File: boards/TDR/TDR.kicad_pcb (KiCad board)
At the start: 4 copper layers, 60 x 37 mm, 131 parts, among them J1 USB_C_Receptacle_USB2.0, J2 SMA, U1 LFE5UM5G-45-CABGA381, U10 W25Q128JVPIQ, U11 93LCxxBxxOT, U12 FT2232HL, U13 MIC5504-3.3YM5, U14 Resistive_Power_Divider, U15 MCP4822, U2 USBLC6-2SC6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

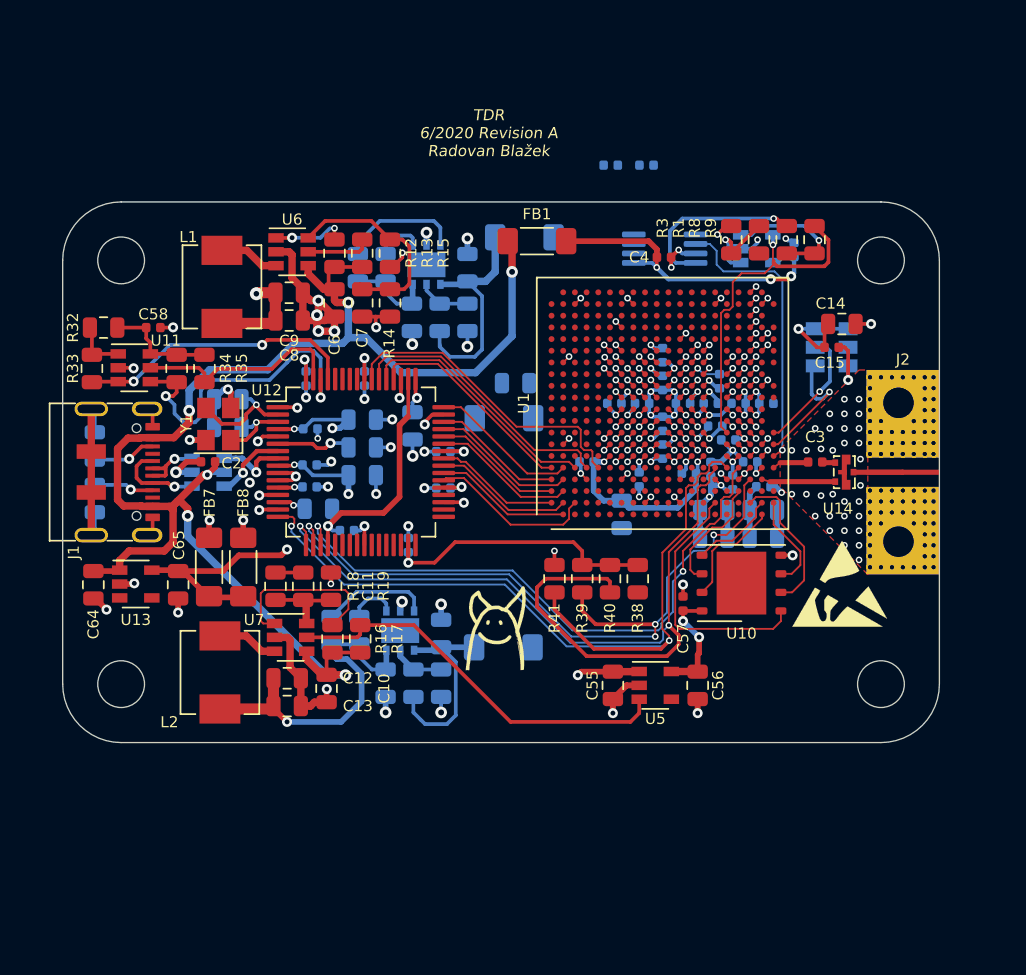
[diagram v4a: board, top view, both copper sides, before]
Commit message: solved DRC errors and routed few more nets
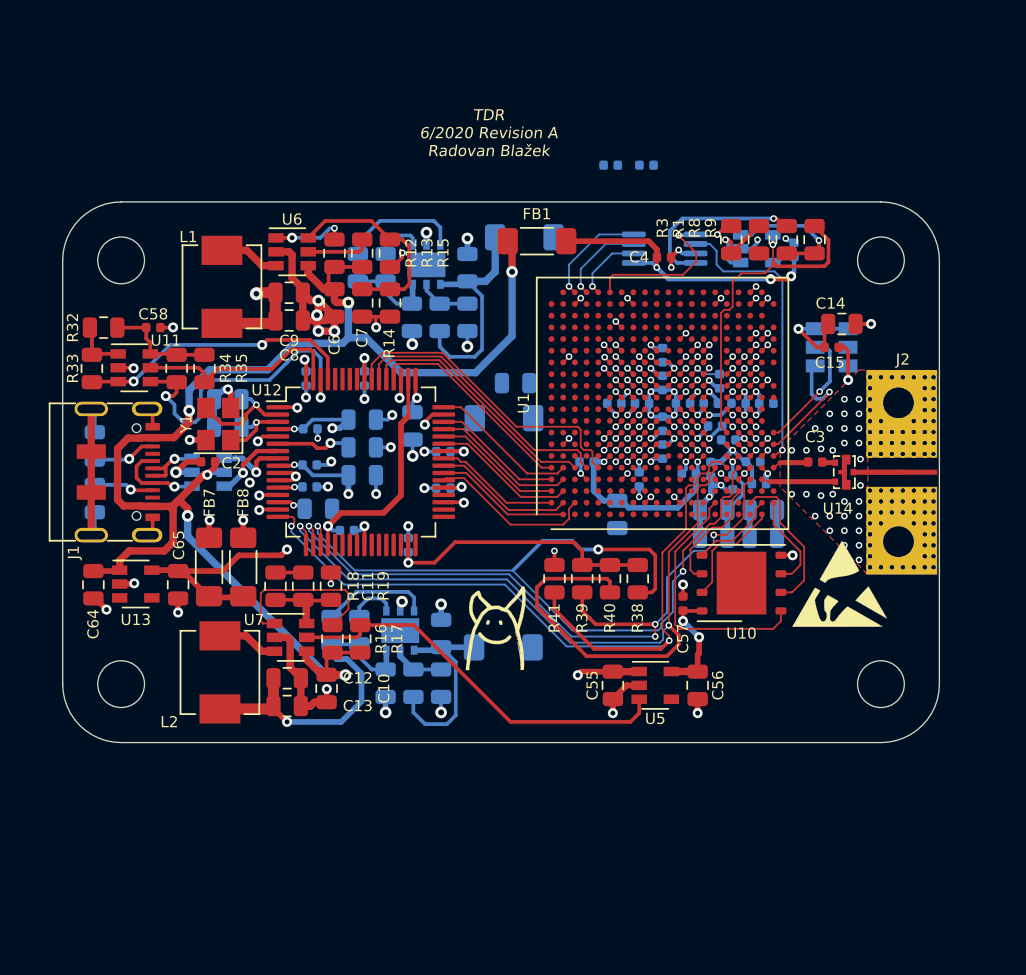
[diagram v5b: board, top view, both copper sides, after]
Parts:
- moved C34 1.84 mm to (154.3, 80.8)
- moved R2 1.62 mm to (154.7, 82.3)
- moved C45 0.30 mm to (145.0, 84.4)
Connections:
- U1 pad C20: Net-(U1-PadC20) -> /SCK
- U1 pad D20: Net-(U1-PadD20) -> /~LDAC
- U1 pad E20: Net-(U1-PadE20) -> /SDI
- U1 pad F10: /FPGA_IO/VCCIO0 -> Net-(U1-PadF10)
- U1 pad F11: /FPGA_IO/VCCIO1 -> Net-(U1-PadF11)
- U1 pad F12: /FPGA_IO/VCCIO1 -> Net-(U1-PadF12)
- U1 pad F20: Net-(U1-PadF20) -> /~CS
- U1 pad F9: /FPGA_IO/VCCIO0 -> Net-(U1-PadF9)
- U1 pad H14: /FPGA_IO/VCCIO2 -> +3V3
- U1 pad H15: /FPGA_IO/VCCIO2 -> +3V3
- U1 pad J15: /FPGA_IO/VCCIO2 -> +3V3
- U1 pad L14: /FPGA_IO/VCCIO3 -> Net-(U1-PadL14)
- U1 pad L15: /FPGA_IO/VCCIO3 -> Net-(U1-PadL15)
- U1 pad L6: /FPGA_IO/VCCIO6 -> Net-(U1-PadL6)
- U1 pad L7: /FPGA_IO/VCCIO6 -> Net-(U1-PadL7)
- U1 pad M15: /FPGA_IO/VCCIO3 -> Net-(U1-PadM15)
- U1 pad M6: /FPGA_IO/VCCIO6 -> Net-(U1-PadM6)
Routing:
- net /TMS: track 41.7 -> 56.3 mm, vias 2 -> 3
- net /~CS: track 0.00 -> 10.8 mm, vias 0 -> 1
- net /SCK: track 0.00 -> 7.35 mm, vias 0 -> 1
- net /~LDAC: track 0.00 -> 6.11 mm, vias 0 -> 1
- net /SDI: track 0.00 -> 4.86 mm, vias 0 -> 1
- net /VCCA: track 3.95 -> 7.12 mm
- net /FPGA_Power/VCCAUX: track 43.3 -> 41.4 mm, vias 8 -> 6
- net /FPGA_IO/VCCIO6: track 1.70 -> 0.00 mm, vias 2 -> 0
- net GND: track 184.6 -> 183.8 mm, vias 178 -> 177

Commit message: add LEDs, only 9 unconnected items remaining
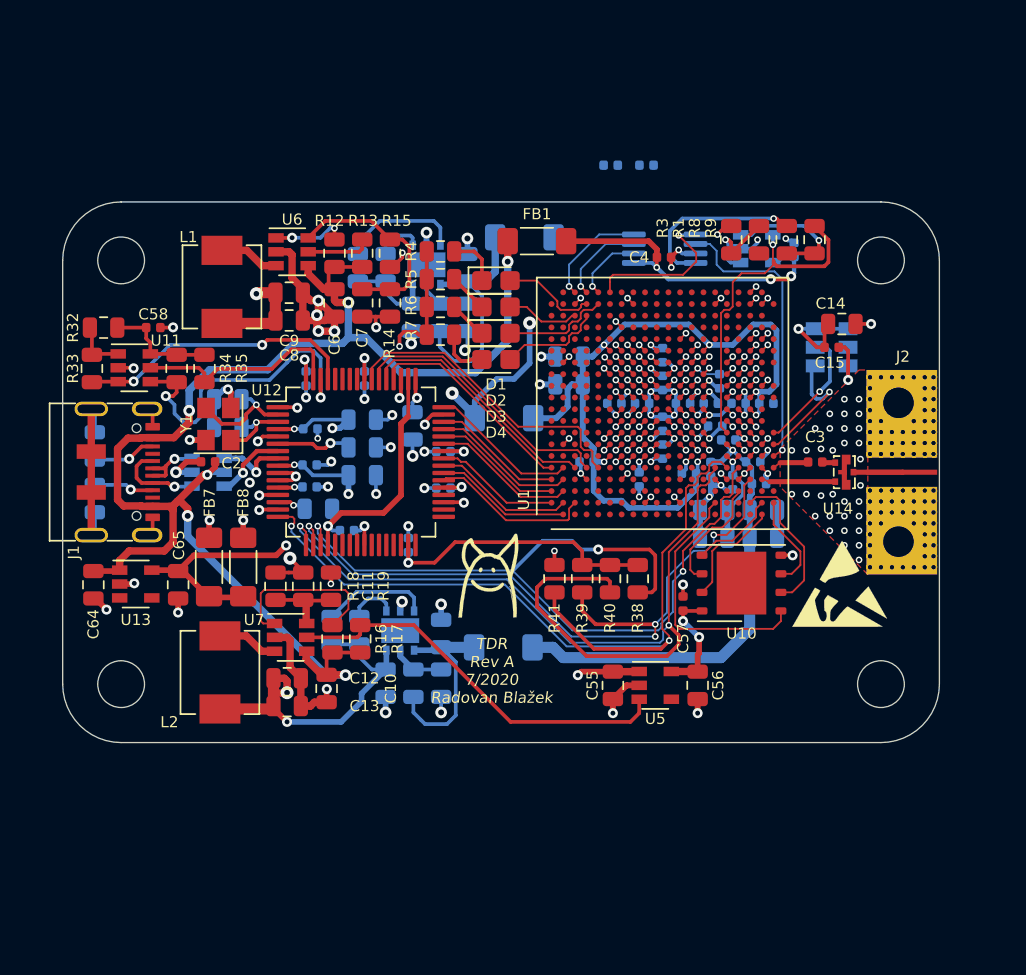
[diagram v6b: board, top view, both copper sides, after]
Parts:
- added D1: LED, LED_SMD:LED_0805_2012Metric_Castellated, F.Cu at (136.7, 68.4)
- added D2: LED, LED_SMD:LED_0805_2012Metric_Castellated, F.Cu at (136.7, 70.2)
- added D3: LED, LED_SMD:LED_0805_2012Metric_Castellated, F.Cu at (136.7, 72.0)
- added D4: LED, LED_SMD:LED_0805_2012Metric_Castellated, F.Cu at (136.7, 73.8)
- added R4: 1k, Resistor_SMD:R_0805_2012Metric, F.Cu at (132.9, 66.4)
- added R5: 1k, Resistor_SMD:R_0805_2012Metric, F.Cu at (132.9, 68.3)
- added R6: 1k, Resistor_SMD:R_0805_2012Metric, F.Cu at (132.9, 70.2)
- added R7: 1k, Resistor_SMD:R_0805_2012Metric, F.Cu at (132.9, 72.1)
- moved C45 9.49 mm to (141.7, 75.5), turned to 180 degrees
- moved C47 4.08 mm to (141.7, 73.6)
- moved G*** 3.63 mm to (136.2, 88.6)
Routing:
- net +2V5: track 39.7 -> 109.8 mm, vias 2 -> 6
- net VCCHTX: track 8.14 -> 32.1 mm
- net +3V3: track 37.3 -> 54.2 mm, vias 7 -> 10
- net GND: track 183.8 -> 195.3 mm, vias 177 -> 180
- net /FPGA_Power/VCCAUX: track 41.4 -> 52.7 mm
- net Net-(D3-Pad2): track 0.00 -> 7.32 mm
- net Net-(D4-Pad2): track 0.00 -> 7.07 mm
- net Net-(D1-Pad2): track 0.00 -> 6.54 mm
- net Net-(D2-Pad2): track 0.00 -> 5.02 mm
- net Net-(D1-Pad1): track 0.00 -> 3.59 mm
- net Net-(D4-Pad1): track 0.00 -> 3.47 mm
- net Net-(D2-Pad1): track 0.00 -> 2.69 mm
- net Net-(D3-Pad1): track 0.00 -> 2.65 mm
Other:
- board text added: "TDR Rev A 7/2020 Radovan Blažek"
- board text removed: "TDR 6/2020 Revision A Radovan Blažek"

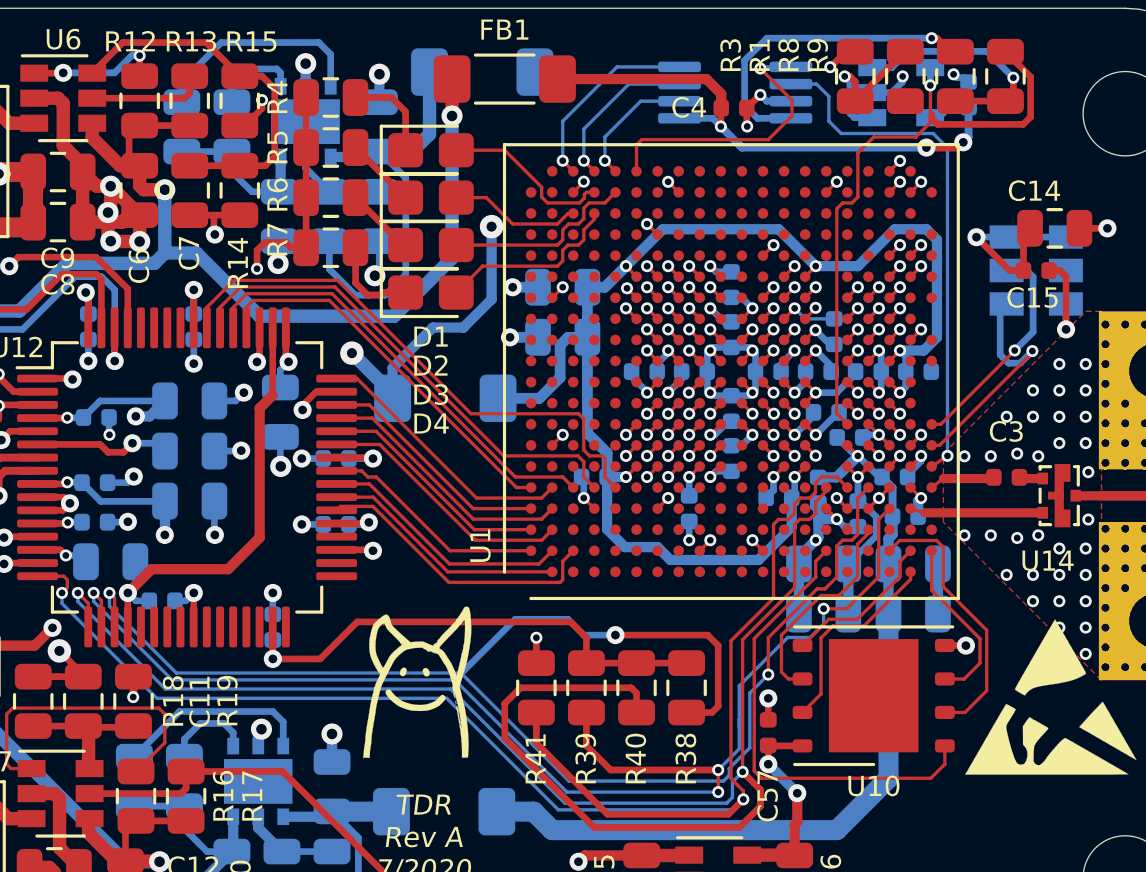
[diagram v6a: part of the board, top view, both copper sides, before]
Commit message: change BGA dogbone stringer width to 0.2 mm, 7 unconncted
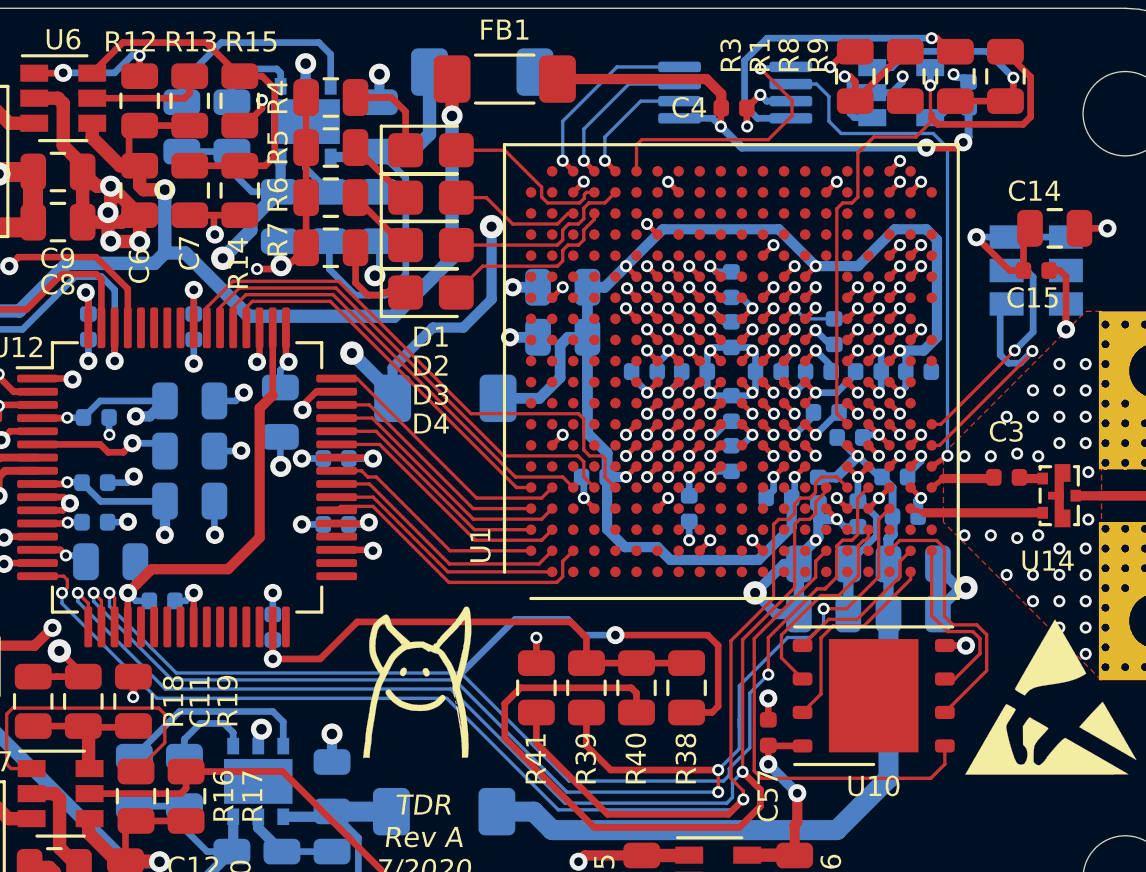
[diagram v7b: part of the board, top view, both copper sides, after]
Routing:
- net +2V5: track 109.8 -> 121.5 mm, vias 6 -> 7
- net GND: track 195.3 -> 202.0 mm, vias 180 -> 182

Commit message: finish routing
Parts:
- removed C36: 1n, Capacitor_SMD:C_0402_1005Metric
- moved C32 23.4 mm to (152.3, 83.3), turned to 180 degrees
- moved C20 0.70 mm to (151.6, 86.7)
- moved C24 0.65 mm to (151.6, 84.7)
- moved C28 0.30 mm to (152.9, 81.9)
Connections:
- U1 pad T10: Net-(U1-PadT10) -> /VCCA
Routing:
- net /VCCA: track 7.12 -> 47.7 mm, vias 1 -> 4
- net GND: track 202.0 -> 203.9 mm, vias 182 -> 183
- net Net-(U1-PadT13): track 1.77 -> 0.00 mm, vias 1 -> 0
- net /~CS: track 10.8 -> 9.34 mm
- net VCCHTX: track 32.1 -> 33.5 mm
- net Net-(C23-Pad1): track 22.0 -> 23.3 mm
- net /TDO: track 49.8 -> 50.6 mm
- net /OUT_B: track 19.9 -> 20.5 mm
- net /OUT_A: track 23.3 -> 22.7 mm
- net Net-(U1-PadT9): track 0.57 -> 0.00 mm, vias 1 -> 0
- net Net-(U1-PadT14): track 0.57 -> 0.00 mm, vias 1 -> 0
- net Net-(U1-PadT11): track 0.57 -> 0.00 mm, vias 1 -> 0
- net Net-(U1-PadT12): track 0.57 -> 0.00 mm, vias 1 -> 0
- net Net-(U1-PadT10): track 0.57 -> 0.00 mm, vias 1 -> 0
- net +2V5: track 121.5 -> 121.7 mm, vias 7 -> 8
